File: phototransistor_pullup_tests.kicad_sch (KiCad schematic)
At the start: 3 parts

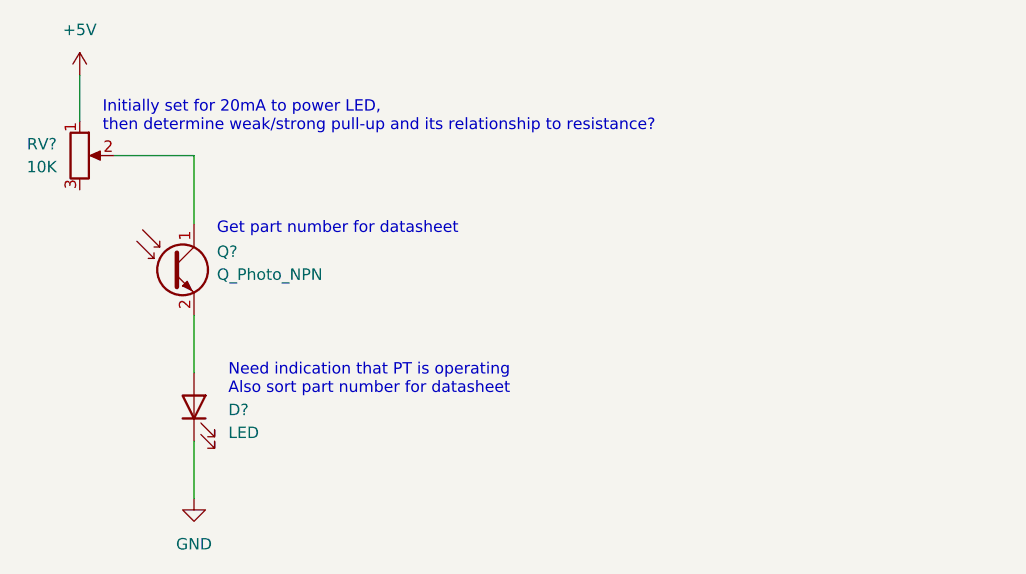
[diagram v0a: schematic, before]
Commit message: v0.1
Added datasheet and initial observations
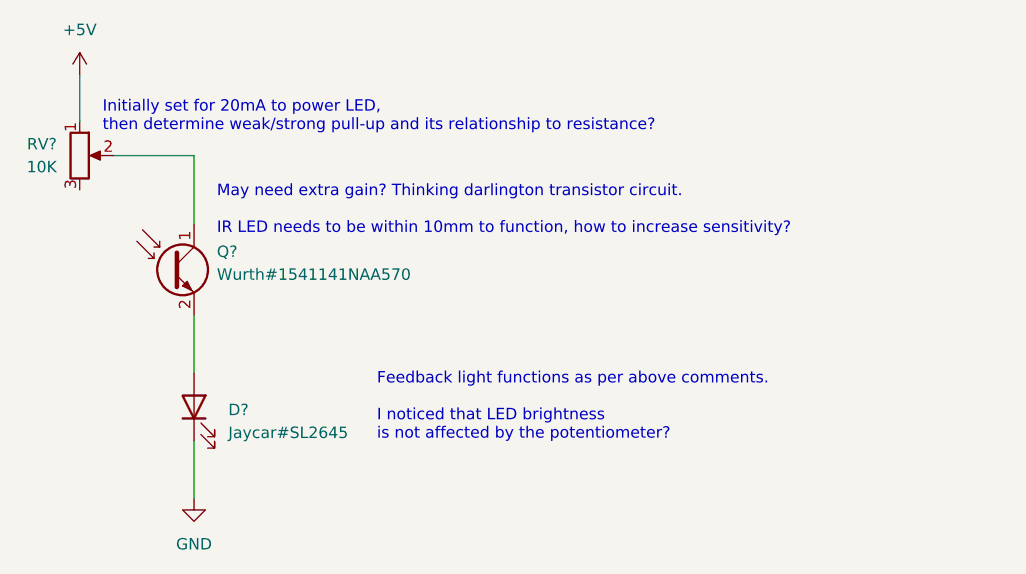
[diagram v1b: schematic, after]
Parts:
- D?: value LED -> Jaycar#SL2645
- Q?: value Q_Photo_NPN -> Wurth#1541141NAA570
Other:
- note added: "Feedback light functions as per above comments. I noticed that LED brightness is not affected by the potentiometer?"
- note added: "May need extra gain? Thinking darlington transistor circuit. IR LED needs to be within 10mm to function, how to increase sensitivity?"
- note removed: "Get part number for datasheet"
- note removed: "Need indication that PT is operating Also sort part number for datasheet"
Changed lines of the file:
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@@
     (stroke (width 0) (type default) (color 0 0 0 0))
   )
-  (text "Need indication that PT is operating\nAlso sort part number for datasheet"
-    (at 143.51 124.46 0)
+  (text "May need extra gain? Thinking darlington transistor circuit.\n\nIR LED needs to be within 10mm to function, how to increase sensitivity?"
+    (at 142.24 106.68 0)
     (effects (font (size 1.27 1.27)) (justify left bottom))
   )
-  (text "Get part number for datasheet" (at 142.24 106.68 0)
+  (text "Feedback light functions as per above comments.\n\nI noticed that LED brightness\nis not affected by the potentiometer?"
+    (at 160.02 129.54 0)
     (effects (font (size 1.27 1.27)) (justify left bottom))
   )
@@
       (effects (font (size 1.27 1.27)) (justify left))
     )
-    (property "Value" "Q_Photo_NPN" (id 1) (at 142.24 111.0106 0)
+    (property "Value" "Wurth#1541141NAA570" (id 1) (at 142.24 111.0106 0)
       (effects (font (size 1.27 1.27)) (justify left))
     )
@@
       (effects (font (size 1.27 1.27)) hide)
     )
-    (property "Datasheet" "~" (id 3) (at 137.16 110.49 0)
+    (property "Datasheet" "https://www.we-online.com/components/products/datasheet/1541141NAA570.pdf" (id 3) (at 137.16 110.49 0)
       (effects (font (size 1.27 1.27)) hide)
     )
@@
       (effects (font (size 1.27 1.27)) (justify right))
     )
-    (property "Value" "LED" (id 1) (at 143.51 128.5874 90)
+    (property "Value" "Jaycar#SL2645" (id 1) (at 143.51 128.5874 90)
       (effects (font (size 1.27 1.27)) (justify right))
     )
@@
       (effects (font (size 1.27 1.27)) hide)
     )
-    (property "Datasheet" "~" (id 3) (at 139.7 125.73 0)
+    (property "Datasheet" "https://www.jaycar.com.au/12v-mini-chrome-bezel-green/p/SL2645" (id 3) (at 139.7 125.73 0)
       (effects (font (size 1.27 1.27)) hide)
     )
@@
     )
     (path "/633ca46e-7ce0-478c-bea5-08ee988e6cf5"
-      (reference "D?") (unit 1) (value "LED") (footprint "")
+      (reference "D?") (unit 1) (value "Jaycar#SL2645") (footprint "")
     )
     (path "/1fdf55e2-bde1-47ac-aa00-362d935b6a35"
-      (reference "Q?") (unit 1) (value "Q_Photo_NPN") (footprint "")
+      (reference "Q?") (unit 1) (value "Wurth#1541141NAA570") (footprint "")
     )
     (path "/4dfcd94b-440e-45d8-ba61-e0e18e3022c5"
